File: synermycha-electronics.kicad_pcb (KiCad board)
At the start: 4 copper layers, 50 x 75 mm, 175 parts, among them IC1 CYPD3177, J12 Conn_01x05, J13 Conn_01x05, J14 Conn_01x05, J15 Conn_01x05, J16 Conn_01x05, J17 CK-JS102011SAQN, J2 Conn_01x02, J3 Conn_01x02, J4 USB_C_Receptacle_USB2.0, J6 A1250WV-S-4P, J7 Conn_01x04, J8 Conn_01x04, Q1 IRLML9301TRPBF, Q2 IRLML9301TRPBF, Q3 IRLML9301TRPBF, Q4 BC847, Q5 BC856, Q7 IRLML9301TRPBF, SW1 DTSM32N, SW2 DTSM32N, SW3 DTSM32N, SW4 DTSM32N, U1 LM1117LDX, U12 MPU-9250, U13 STM32F446RETx, U14 STM14_SW, U2 LDFM33PVR, U3 RN4871U-V_RM118, U4 DRV8835, U5 MCP73213, U6 ETA3000, Y1 16Mhz, 18pF

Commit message: Dodano grafiki do płytek enkodera
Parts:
- moved C30 2.06 mm to (39.1, 133.5), turned to 180 degrees
- moved C17 0.10 mm to (40.0, 186.9)
- moved C18 0.10 mm to (39.0, 186.9)
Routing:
- net /Power Section/CYPD_+3V3: track 27.0 -> 32.9 mm
- net Net-(Q5-Pad2): track 4.64 -> 8.22 mm
- net /Distance Sensors/VL53L0x_~XSHUT[1]: track 14.8 -> 13.5 mm
- net Net-(D7-Pad1): track 28.2 -> 29.1 mm
- net Net-(C15-Pad1): track 18.2 -> 17.5 mm
- net /Power Section/BATT+: track 22.4 -> 22.9 mm
- net GND: track 18.3 -> 18.4 mm, vias 74 -> 151
- net (no net): vias 0 -> 9
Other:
- board text added: "v2.0 by: s.mroz b.ostr s.dac"
- board text removed: "v2.0 by: s.mroz b.ostr s.dac @PWr 2020"

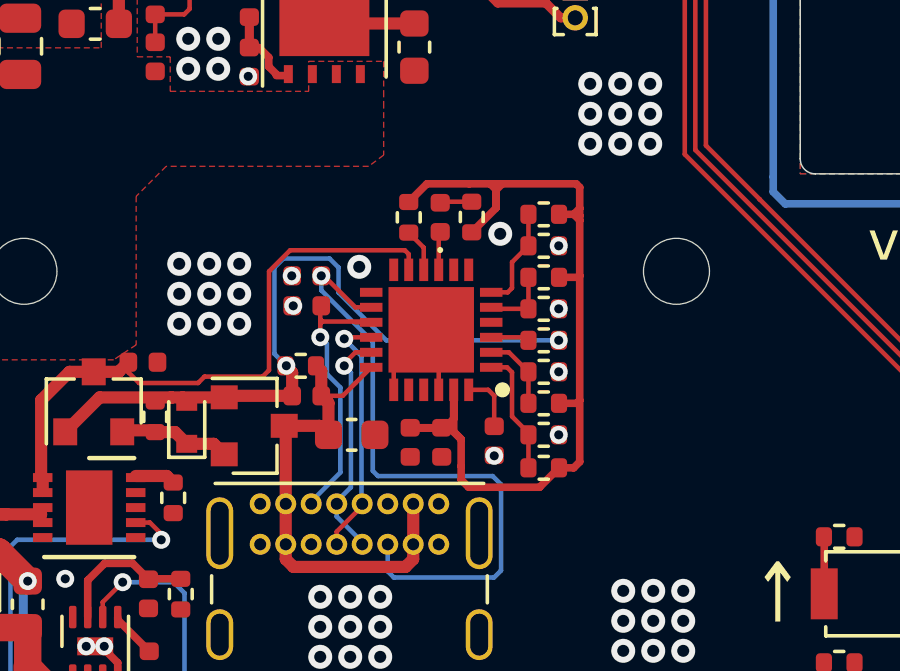
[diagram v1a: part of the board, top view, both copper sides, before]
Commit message: Dodano więcej przelotek do masy
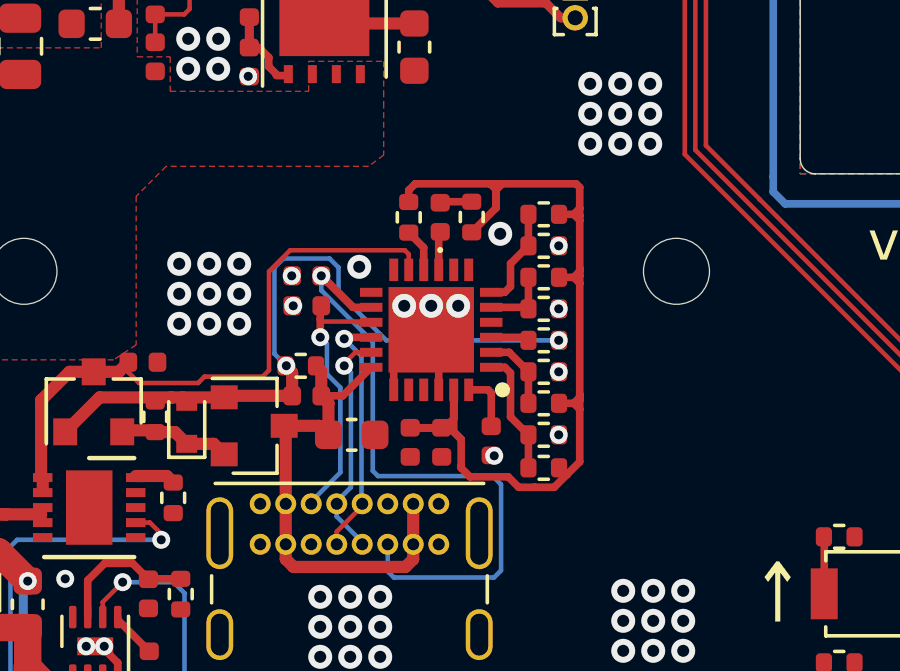
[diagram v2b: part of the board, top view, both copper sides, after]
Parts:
- moved C16 0.10 mm to (41.7, 186.9)
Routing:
- net Net-(C14-Pad1): track 21.4 -> 23.5 mm
- net /Power Section/CYPD_+3V3: track 32.9 -> 34.6 mm
- net Net-(IC1-Pad2): track 2.56 -> 4.07 mm
- net Net-(C5-Pad1): track 9.67 -> 10.3 mm
- net GND: vias 151 -> 154

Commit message: Estetyka
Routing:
- net GND: vias 154 -> 163
- net (no net): vias 9 -> 0

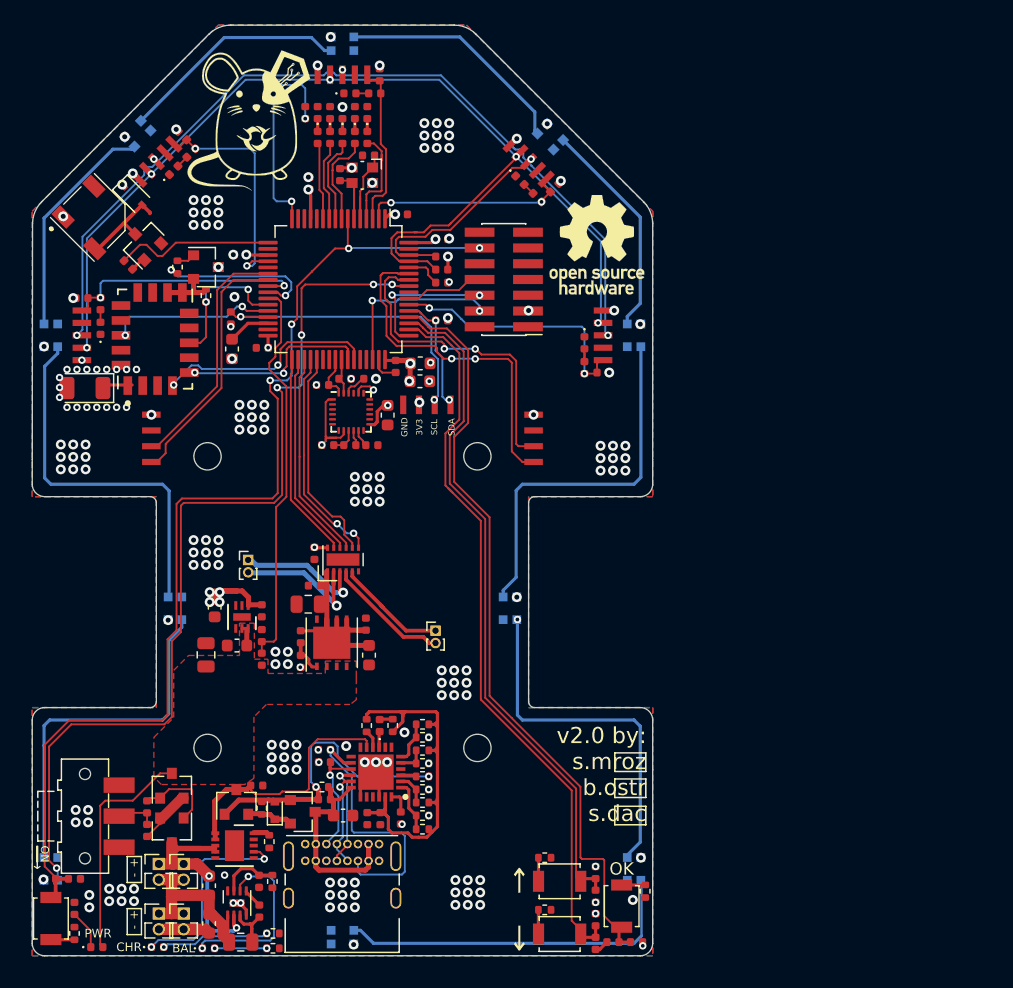
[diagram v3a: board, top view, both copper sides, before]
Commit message: Zmiany w drc lepiej oddające możliwości produkcyjne, estetyczne zmiany
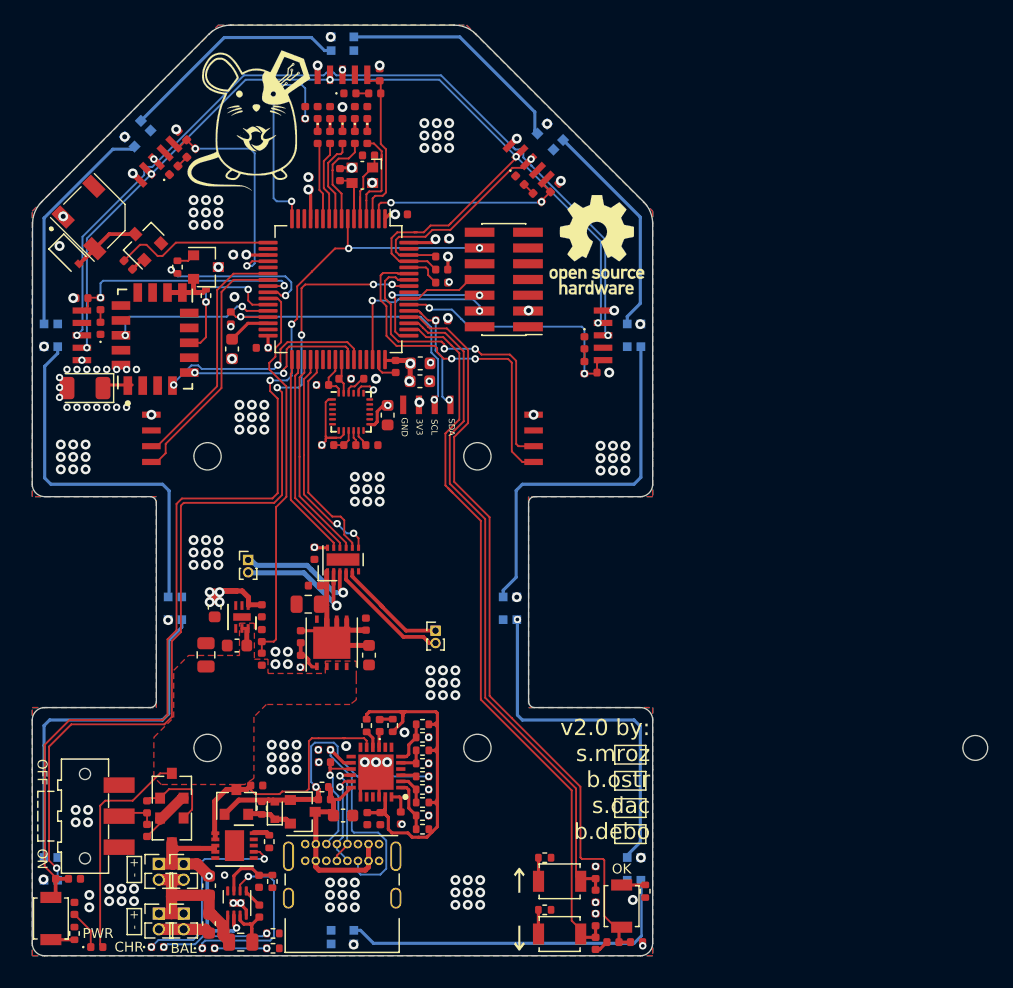
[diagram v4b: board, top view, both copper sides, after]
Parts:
- removed the G*** at (45.0, 163.0)
- added G***: LOGO, graphics:SynerMycha_Synergia_silk_screen_26.4x30.3, B.Cu at (37.0, 141.0)
- added G***: LOGO, graphics:Synergia_logo_horizontal_17.8x12.6mm, B.Cu at (48.2, 170.0)
- added REF**: mocowanie_silników, mocowanie_silników:mocowanie_silników, F.Cu at (98.7, 168.5)
- added REF**: KiCad-Logo2_6mm_SilkScreen, Symbol:KiCad-Logo2_6mm_SilkScreen, B.Cu at (54.5, 188.4)
- moved D1 6.99 mm to (15.0, 141.5)
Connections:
- net Net-(IC1-Pad16) renamed /Power Section/D-
- net Net-(IC1-Pad17) renamed /Power Section/D+
- U6 pad 9: GND -> (no net)
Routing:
- net Net-(C14-Pad1): track 23.5 -> 20.2 mm
- net Net-(BZ1-Pad2): track 7.52 -> 6.72 mm
- net Net-(C19-Pad1): track 20.6 -> 21.2 mm
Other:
- net class Default: clearance 0.2 -> 0.1524; trace_width 0.25 -> 0.1524
- rule trace_clearance: 0.2 -> 0.1524
- board text added: "OFF"
- board text added: "v2.0 by: s.mroz b.ostr s.dac b.debo"
- board text removed: "v2.0 by: s.mroz b.ostr s.dac"

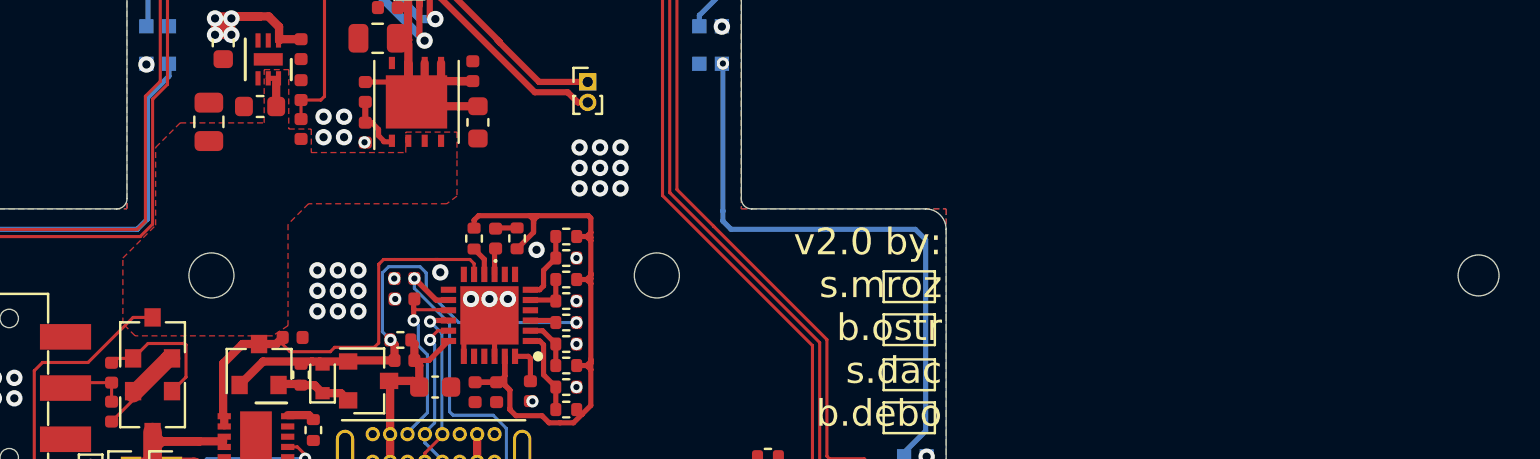
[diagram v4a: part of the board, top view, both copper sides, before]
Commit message: Zmieniono miejsce modelu silników na płytce
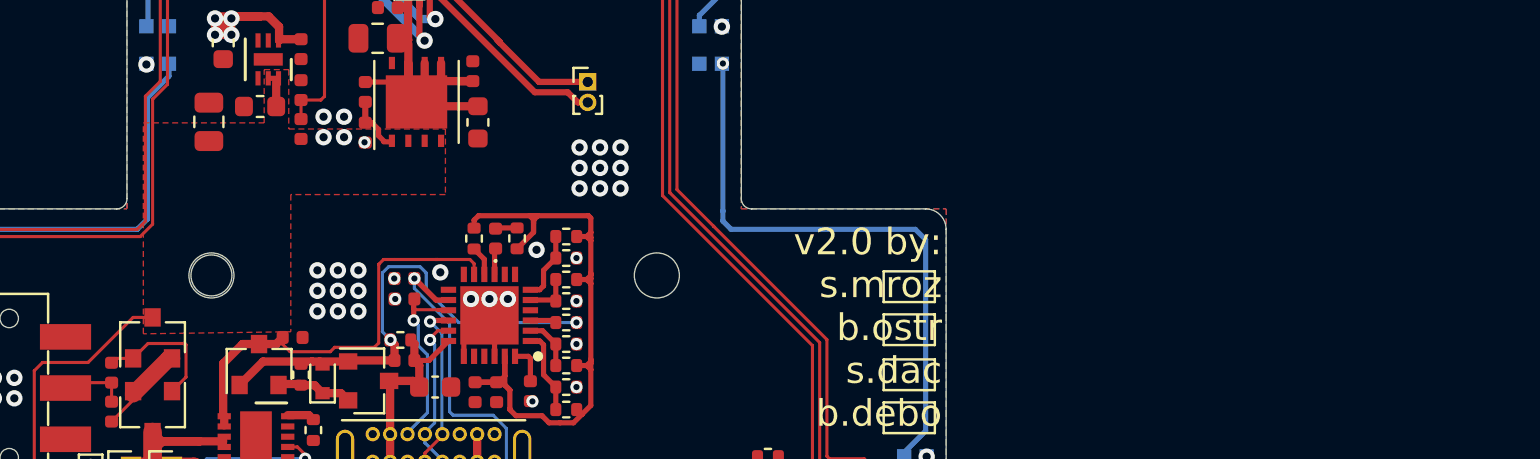
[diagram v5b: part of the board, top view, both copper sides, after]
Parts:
- moved REF** 61.9 mm to (36.9, 168.5)
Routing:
- added copper zone on In2.Cu, net GND
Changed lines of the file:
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@@
     (34 B.Paste user hide)
     (35 F.Paste user hide)
-    (36 B.SilkS user hide)
-    (37 F.SilkS user)
+    (36 B.SilkS user)
+    (37 F.SilkS user hide)
     (38 B.Mask user hide)
     (39 F.Mask user hide)
@@
   )
   (setup
-    (last_trace_width 0.3048)
+    (last_trace_width 0.1524)
     (user_trace_width 0.1524)
     (user_trace_width 0.2032)
@@
     (trace_clearance 0.1524)
     (zone_clearance 0.1524)
-    (zone_45_only no)
+    (zone_45_only yes)
     (trace_min 0.1524)
     (via_size 0.8)
@@
   )
   (module mocowanie_silników:mocowanie_silników (layer F.Cu)
-    (at 98.7442 168.4992 180)
+    (at 36.8692 168.4992 180)
     (fp_text reference REF** (at 16 5.75 180) (layer F.SilkS) hide
       (effects (font (size 1 1) (thickness 0.15)))
@@
     (connect_pads (clearance 0.1524))
     (min_thickness 0.1524)
-    (fill yes (arc_segments 32) (thermal_gap 0.2032) (thermal_bridge_width 0.2032))
+    (fill yes (arc_segments 32) (thermal_gap 0.2032) (thermal_bridge_width 0.2032) (smoothing fillet) (radius 0.254))
     (polygon
       (pts
@@
     )
   )
-  (zone (net 20) (net_name "/Power Section/VCC") (layer F.Cu) (hatch edge 0.508)
+  (zone (net 1) (net_name GND) (layer In2.Cu) (hatch edge 0.508)
     (priority 1)
     (connect_pads (clearance 0.1524))
+    (min_thickness 0.1524)
+    (fill yes (arc_segments 32) (thermal_gap 0.2032) (thermal_bridge_width 0.2032))
+    (polygon
+      (pts
+        (xy 42 195) (xy 32 195) (xy 32 180) (xy 42 180)
+      )
+    )
+  )
+  (zone (net 20) (net_name "/Power Section/VCC") (layer F.Cu) (hatch edge 0.508)
+    (priority 1)
+    (connect_pads yes (clearance 0.1524))
     (min_thickness 0.254)
-    (fill yes (arc_segments 32) (thermal_gap 0.508) (thermal_bridge_width 0.508))
+    (fill yes (arc_segments 32) (thermal_gap 0.508) (thermal_bridge_width 0.508) (smoothing chamfer) (radius 0.5))
     (polygon
       (pts
-        (xy 29.9 174.1) (xy 31 174.1) (xy 31 175.25) (xy 35.615059 175.25) (xy 35.615059 174.25)
-        (xy 38.115059 174.25) (xy 38.115059 175.25) (xy 38.115059 175.625) (xy 38.115059 177.375) (xy 37.615059 177.75)
-        (xy 30.865059 177.75) (xy 29.865059 178.75) (xy 29.865059 183.7) (xy 29.115059 184.2) (xy 22.4 184.2)
-        (xy 21.8 183.6) (xy 21.8 180.4) (xy 23.4 178.8) (xy 23.4 175) (xy 24.6 173.8)
-        (xy 28.7 173.8) (xy 28.7 171.2) (xy 29.9 171.2)
+        (xy 29.9 174.1) (xy 37.55 174.1) (xy 37.55 177.3) (xy 30 177.3) (xy 30 184)
+        (xy 22.8 184.1) (xy 22.8 173.8) (xy 28.7 173.8) (xy 28.7 171.2) (xy 29.9 171.2)
       )
     )
